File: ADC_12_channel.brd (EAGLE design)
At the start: 160 x 127 mm, 165 parts, among them K1 691131710003, K2 691101710002, K3 691101710002, K4 691101710002, K5 691101710002, K6 691101710002, K7 691101710002, K8 691101710002, K9 691101710002, U1 AD7864ASZ-1, U10 TL082D, U11 +12v, U12 V_REG_317SMD, U2 AD7864ASZ-1, U3 TL082D, U4 TL082D, U5 TL082D, U6 TL082D, U7 TL082D, U8 TL082D, U9 TL082D, X1 QTE-040

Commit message: Supply sorting commit
Sorted I/p +- 12V supply, 5V pending
changed Resistor package from 0805 to 1206 because its cheap, easy to handle, and easyly available

Update of R package done for 1st two input channels
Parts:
- removed U$1: LM3480IM4, SparkFun-PowerIC:SOT23-3
- removed U11: +12v, rathin_lib:TO-252
- added IC1: LM317BD2T, rathin_Vreg_D2pack:D2PACK
- added IC2: LM317BD2T, v-reg:D2PACK
- R11, R12, R13, R14, R15, R16, R24, R25, R26, R31, R36, R37: device resistor:M0805 -> resistor:M1206
- moved R57 10.6 mm to (76.7, -12.8), turned to 0 degrees
- moved C51 6.33 mm to (66.7, -15.7), turned to 0 degrees
- moved R56 5.28 mm to (72.1, -18.5), turned to 0 degrees
- moved C49 4.22 mm to (72.0, -15.8), turned to 180 degrees
- moved R59 3.91 mm to (66.7, -18.6)
- moved C48 2.70 mm to (76.7, -9.55)
- moved C43 2.53 mm to (69.8, 14.7)
- moved R50 2.39 mm to (109.0, 7.87)
- moved C52 1.15 mm to (60.6, -13.5)
- moved R55 0.94 mm to (76.7, -16.8)
- moved U10 0.31 mm to (96.3, -12.2)
- moved R53 0.25 mm to (113.8, 6.10)
- moved R65 0.24 mm to (94.5, -23.9)
- moved R41 0.18 mm to (66.1, 37.4)
- moved C45 0.17 mm to (95.2, 9.91)
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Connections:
- net GND2: now also IC1.1, IC2.2; no longer U$1.3, U11.1
- net N$35: now also IC1.3; no longer U11.3
- net N$36: now also IC2.1; no longer U$1.2
- net VCC_12+: now also IC2.3; no longer U$1.1
- net VCC_12-: now also IC1.2; no longer U11.2
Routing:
- net N$82: track 0.00 -> 22.6 mm
- net AGND: track 120.4 -> 131.8 mm
- net N$61: track 19.8 -> 11.6 mm
- net VDD: track 24.3 -> 16.3 mm
- net ADC8: track 0.00 -> 6.39 mm
- net VCC_12-: track 0.00 -> 4.94 mm
- net N$63: track 4.85 -> 0.00 mm
- net N$68: track 15.6 -> 14.3 mm
- net N$29: track 19.7 -> 18.9 mm

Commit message: R & C package update
Updated all R to 1206
Updated all input stage C of 0.1u to 0603 package
All 47uF to 1206 package
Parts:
- removed JP2, JP3, JP5: (no value), SparkFun-Retired:1X02
- added R74: 0, resistor:M1206
- C1, C10, C11, C12, C13, C14, C15, C16, C17, C18, C19, C2, C22, C30, C31, C32, C33, C34, C35, C36, C37, C38, C39, C40, C41, C42, C43, C44, C45, C46, C47, C48, C49, C5, C50, C51, C52, C53, C54, C55, C56, C57, C58, C59, C6, C9: device rcl:C0805 -> rcl:C0603K
- C4, C8: device rcl:C0603K -> rcl:C1206K
- R10, R27, R28, R29, R30, R32, R33, R34, R35, R38, R39, R40, R41, R42, R43, R44, R45, R47, R48, R49, R50, R51, R53, R54, R55, R56, R57, R59, R60, R61, R62, R63, R64, R65: device resistor:M0805 -> resistor:M1206
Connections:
- removed net N$18: JP2.2, JP3.1, U1.11
- removed net N$25: JP5.1, R72.1, U2.11
- net DGND: now also R74.2; no longer JP2.1
- net N$19: now also R74.1, U1.11; no longer JP3.2
- net N$26: now also R72.1, U2.11; no longer JP5.2
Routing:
- net N$61: track 11.6 -> 12.4 mm
- net N$68: track 14.3 -> 15.0 mm
- net N$60: track 20.4 -> 21.0 mm

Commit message: Supply Finally sorted out!
arranging supply components
Working on realigning resistors of input stage
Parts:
- added R75: 100k, rcl:R1206
- moved C22 442.6 mm to (228.9, 64.0)
- moved C59 442.6 mm to (228.9, 70.4)
- moved CONVST 442.6 mm to (221.2, 48.6)
- moved IC1 442.6 mm to (213.4, 39.8)
- moved IC2 442.6 mm to (201.4, 39.8)
- moved R20 442.6 mm to (221.7, 43.9)
- moved R71 442.6 mm to (221.7, 37.9)
- moved R73 442.6 mm to (221.7, 31.9)
- moved R74 442.6 mm to (197.9, 25.9)
- moved U12 442.6 mm to (222.6, 56.6)
- moved D1 378.0 mm to (140.2, 90.0)
- moved D2 374.9 mm to (140.6, 79.9)
- moved C21 330.3 mm to (176.6, 160.4)
- moved C26 330.3 mm to (150.0, 115.9)
- moved C28 330.3 mm to (174.1, 146.4)
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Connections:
- removed net 0.8V: R21.2, R22.1, R23.1
- new net 3V: R21.2, R22.1, R23.1, R75.2
- net VCC_5+: now also R75.1

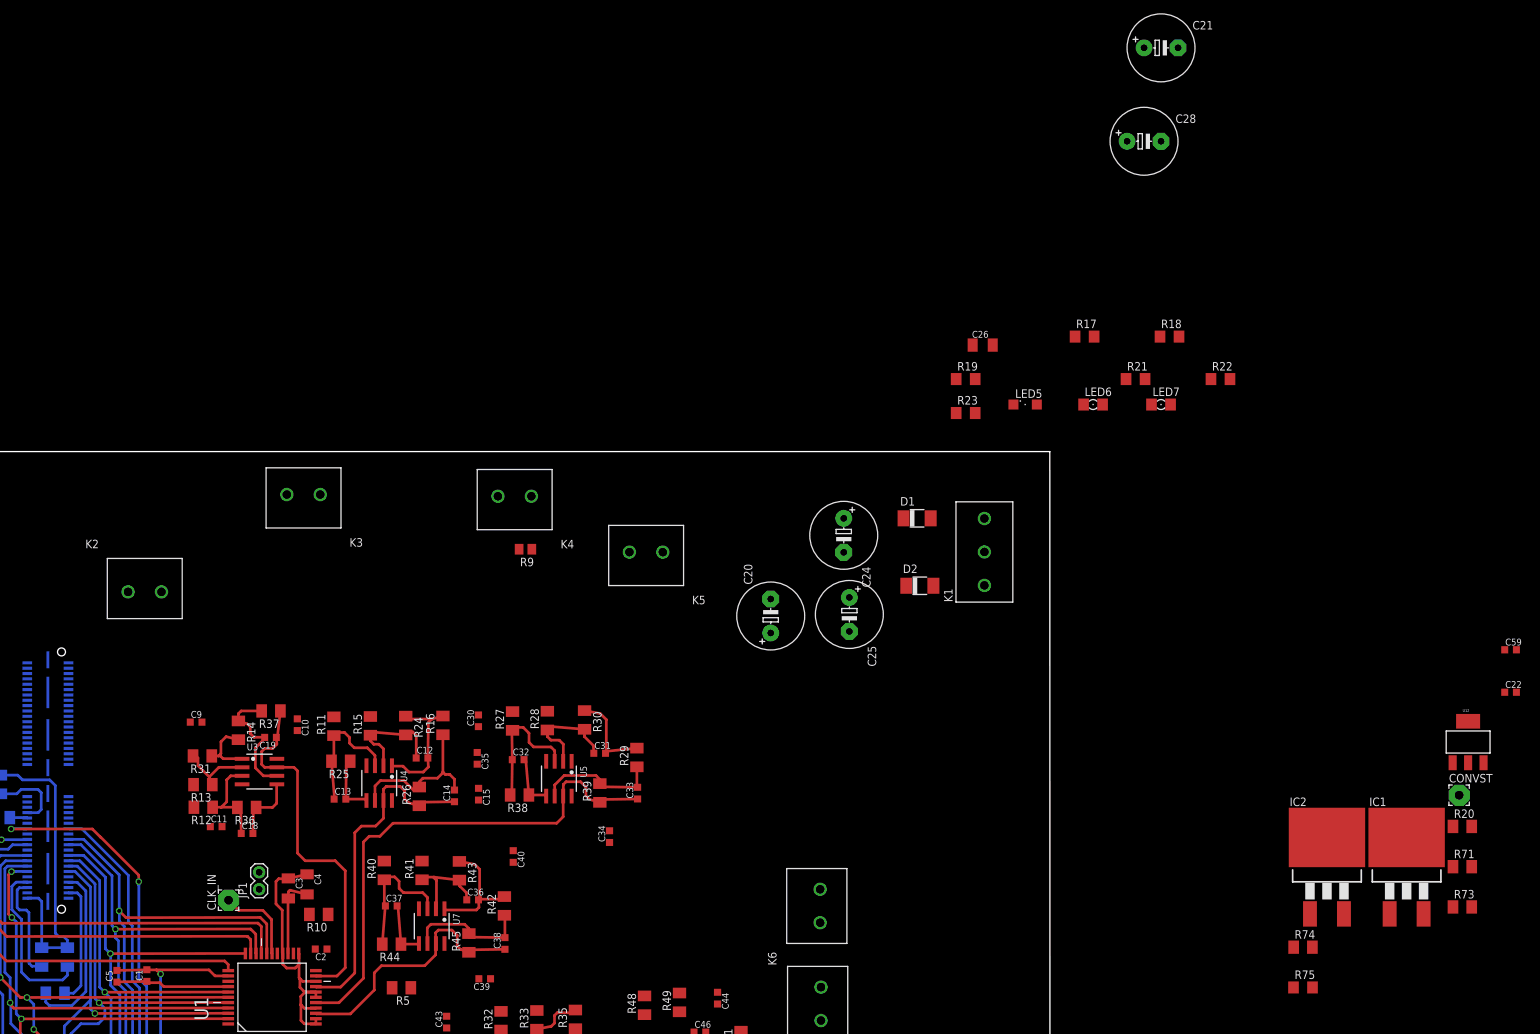
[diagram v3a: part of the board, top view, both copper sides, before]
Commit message: Layout of Supply DONE!
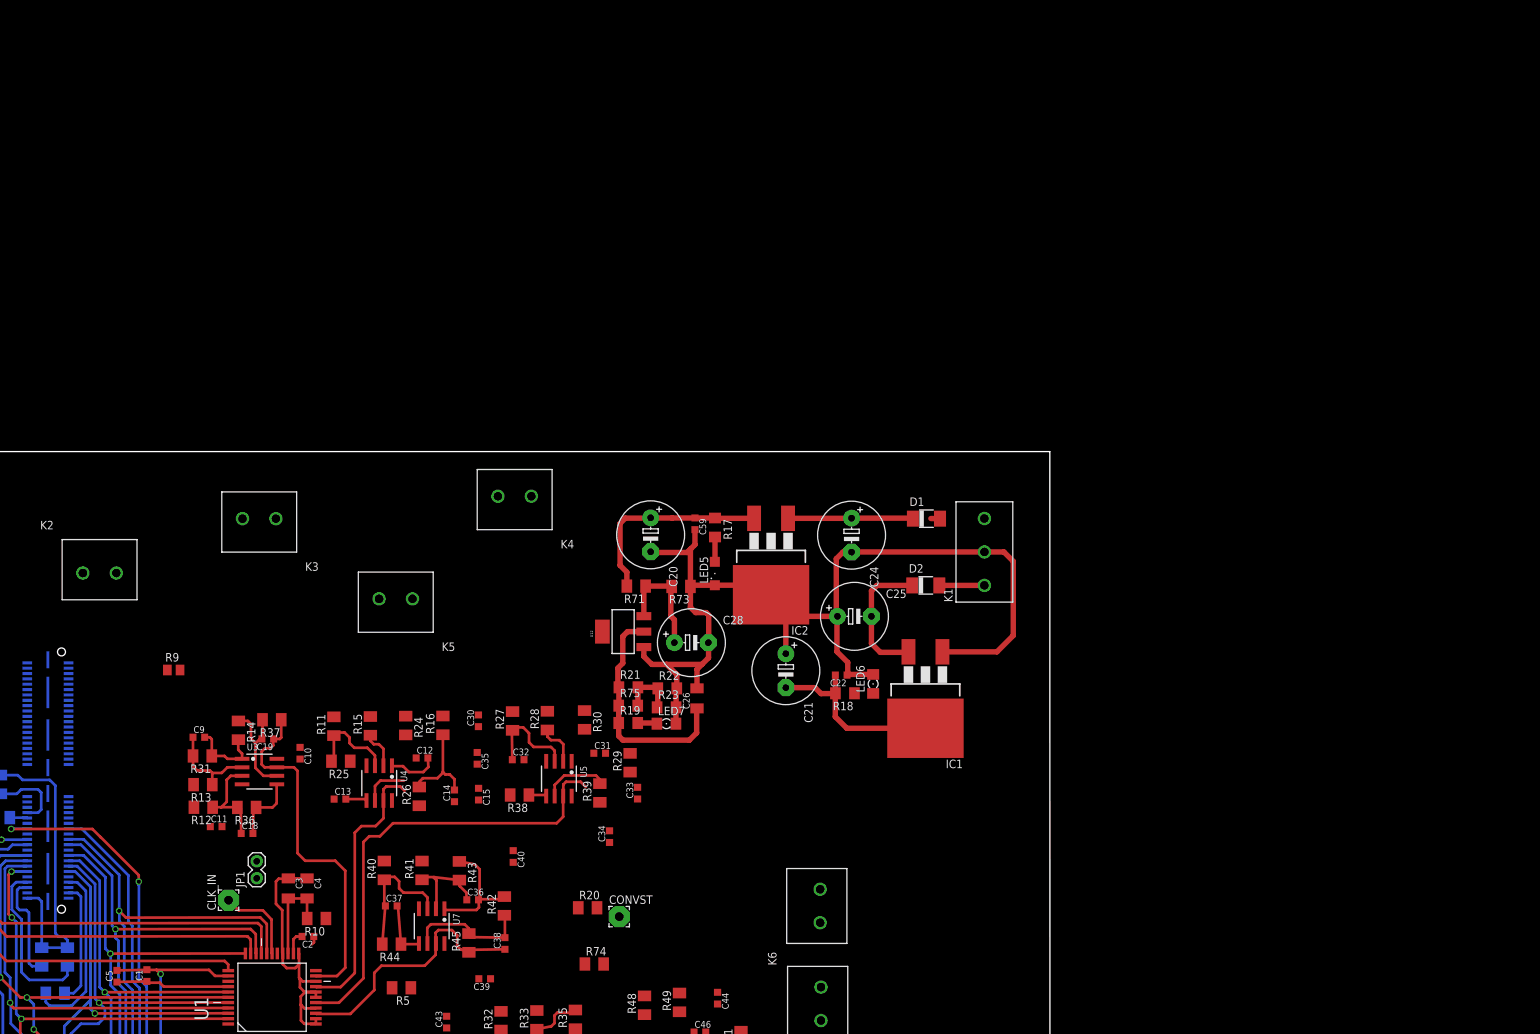
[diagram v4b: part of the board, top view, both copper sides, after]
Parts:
- moved R20 131.4 mm to (90.9, 31.8)
- moved R71 130.5 mm to (98.1, 79.9), turned to 180 degrees
- moved U12 127.4 mm to (96.2, 73.1), turned to 90 degrees
- moved CONVST 126.9 mm to (95.6, 30.5)
- moved R73 126.3 mm to (104.9, 79.8), turned to 180 degrees
- moved C59 123.4 mm to (106.9, 89.2), turned to 270 degrees
- moved R75 109.4 mm to (97.0, 62.0)
- moved C21 108.7 mm to (120.5, 67.2), turned to 270 degrees
- moved R74 106.0 mm to (91.9, 23.4)
- moved C28 101.0 mm to (106.4, 71.4)
- moved C22 100.1 mm to (128.8, 66.6), turned to 180 degrees
- moved R22 94.8 mm to (102.8, 64.6)
- moved IC2 92.9 mm to (118.3, 81.1), turned to 180 degrees
- moved R21 88.8 mm to (97.0, 64.7)
- moved LED7 88.0 mm to (102.7, 59.3)
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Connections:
- removed net GND2: C20.-, C21.+, C22.1, C24.-, C25.+, C26.2, C28.-, C59.2, IC1.1, IC2.2, K1.2, LED5.C, LED6.C, LED7.C, R22.2, R23.2, R73.1, U12.1
- net DGND: now also C20.-, C21.+, C22.1, C24.-, C25.+, C26.2, C28.-, C59.2, IC1.1, IC2.2, K1.2, LED5.C, LED6.C, LED7.C, R22.2, R23.2, R73.1, U12.1
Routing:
- net DGND: track 17.0 -> 172.8 mm
- net VCC_5+: track 0.00 -> 34.7 mm
- net VCC_12+: track 0.00 -> 30.2 mm
- net VCC_12-: track 5.01 -> 33.3 mm
- net N$35: track 0.00 -> 20.4 mm
- net N$36: track 0.00 -> 18.7 mm
- net 5V: track 0.00 -> 17.2 mm
- net N$59: track 13.6 -> 0.00 mm
- net N$34: track 19.6 -> 7.92 mm
- net N$58: track 17.4 -> 6.42 mm
- net N$33: track 16.8 -> 6.41 mm
- net AGND: track 131.8 -> 121.4 mm
- net ADC3: track 78.9 -> 69.6 mm
- net N$65: track 19.1 -> 9.88 mm
- net ADC2: track 50.2 -> 41.3 mm
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
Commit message: Conversion ST signal, supply & area
-Added isolating resistor in CONVST signal coming from header/processor
-Defined boundry of the baord
- Relocated and reorianted the supply
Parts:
- removed CONV_ST1: (no value), wirepad:3,17/1,3
- added CONV_ST2: (no value), wirepad:3,17/1,3
- added R76: 0, resistor:M1206
- moved C20 54.0 mm to (105.9, 33.8), turned to 0 degrees
- moved R71 50.6 mm to (113.6, 31.6), turned to 270 degrees
- moved U12 49.7 mm to (120.4, 29.7), turned to 180 degrees
- moved C59 48.8 mm to (104.2, 40.4), turned to 0 degrees
- moved R19 47.0 mm to (134.0, 30.5), turned to 90 degrees
- moved R75 46.7 mm to (131.4, 30.5), turned to 90 degrees
- moved R21 46.7 mm to (128.7, 30.5), turned to 90 degrees
- moved R17 45.5 mm to (104.8, 43.4), turned to 0 degrees
- moved R73 42.4 mm to (113.6, 38.4), turned to 270 degrees
- moved K1 41.8 mm to (108.5, 83.7), turned to 180 degrees
- moved D1 40.9 mm to (103.5, 75.1), turned to 90 degrees
- moved LED7 39.1 mm to (134.1, 36.2), turned to 90 degrees
- moved R23 38.7 mm to (131.7, 36.2), turned to 90 degrees
- moved R22 38.5 mm to (128.9, 36.3), turned to 90 degrees
- moved LED5 38.4 mm to (111.7, 43.4), turned to 180 degrees
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- renumbered CONVST to CONVST1
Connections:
- removed net N$42: CONVST1.1, R20.2
- new net N$18: CONVST1.1, R20.1, U1.3
- new net N$25: CONV_ST2.1, R76.1, U2.3
- net CONVST: now also R20.2, R76.2; no longer CONV_ST1.1, R20.1, U1.3, U2.3
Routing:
- net CONVST: track 0.00 -> 92.4 mm, vias 0 -> 3
- net VCC_3+: track 0.00 -> 43.8 mm, vias 0 -> 2
- net AGND: track 121.4 -> 111.1 mm
- net N$55: track 15.9 -> 8.27 mm
- net DVDD: track 53.5 -> 54.3 mm
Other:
- board size 160 x 127 mm -> 148.1 x 127 mm

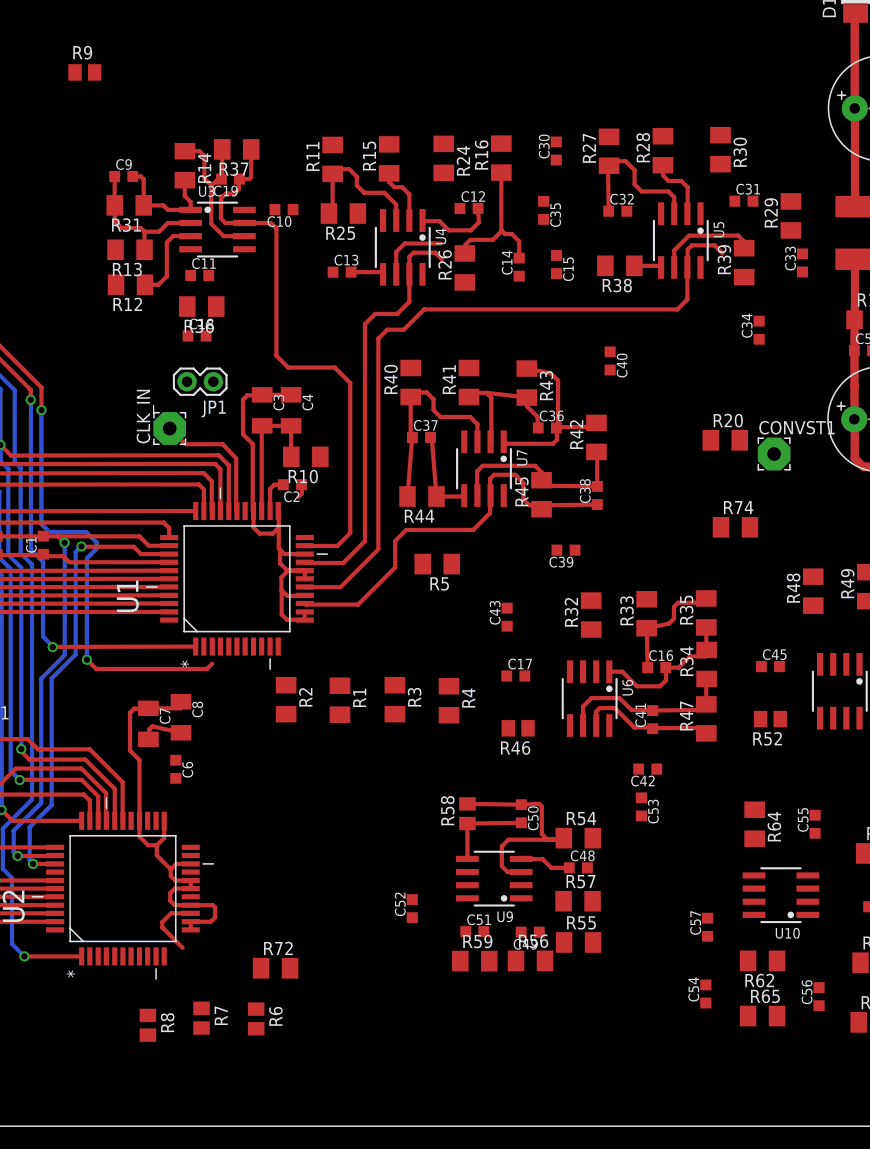
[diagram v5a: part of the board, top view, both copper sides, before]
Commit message: ADC-1 Opamp component arrangement FINALIZED!
Uniformly arranged all component of Opamps 1-4
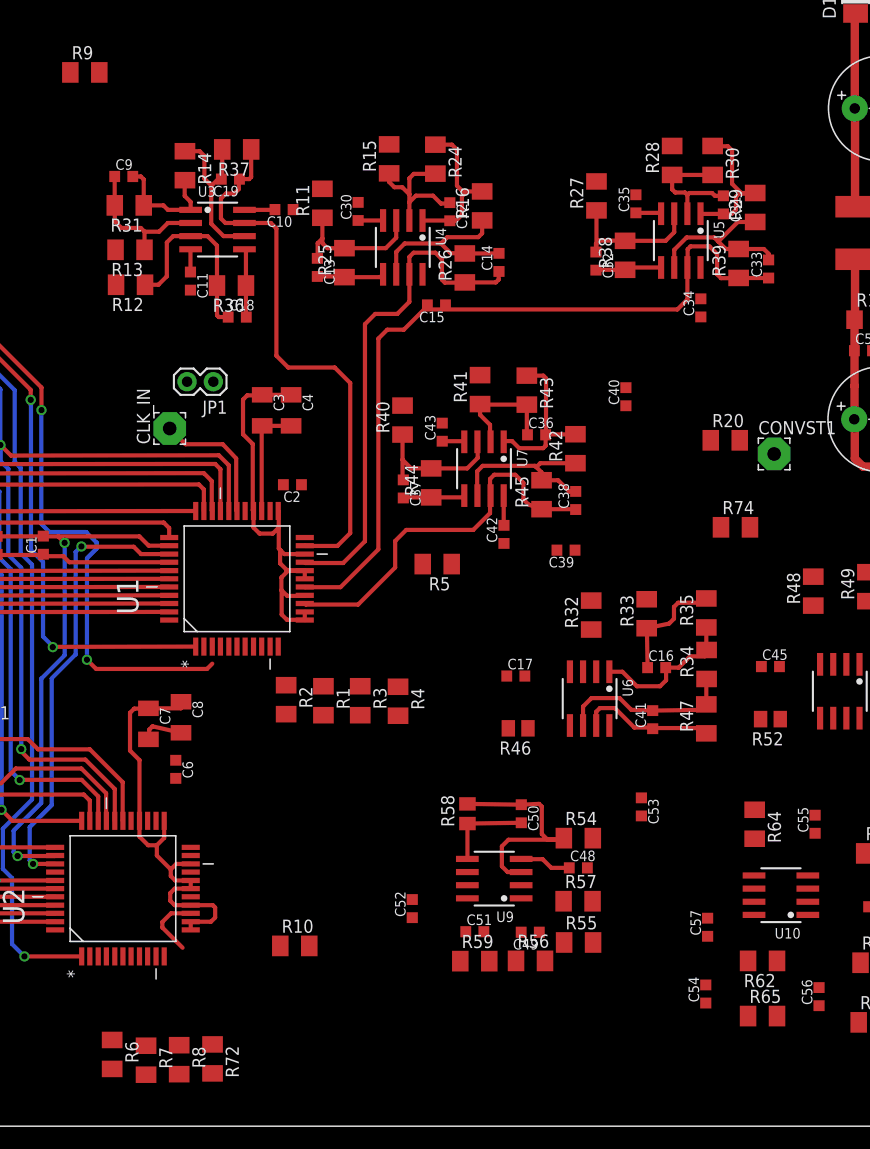
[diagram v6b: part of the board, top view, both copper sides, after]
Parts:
- R6, R7, R8, R9: device resistor:M0805 -> resistor:M1206
- moved R10 47.3 mm to (49.3, -17.1), turned to 0 degrees
- moved C42 26.6 mm to (69.5, 22.7), turned to 90 degrees
- moved C30 20.0 mm to (55.4, 53.9)
- moved C43 19.0 mm to (63.5, 32.6)
- moved R6 14.3 mm to (31.6, -27.6)
- moved C15 12.2 mm to (63.0, 44.9), turned to 180 degrees
- moved R72 10.7 mm to (41.3, -28.0), turned to 270 degrees
- moved C35 8.94 mm to (82.2, 54.6), turned to 90 degrees
- moved R7 6.73 mm to (34.9, -28.1)
- moved C34 6.04 mm to (88.5, 44.6)
- moved C37 5.28 mm to (59.8, 27.1), turned to 270 degrees
- moved C32 5.27 mm to (78.4, 49.1), turned to 270 degrees
- moved R16 4.98 mm to (67.4, 54.4)
- moved R4 4.93 mm to (59.3, 6.55)
- moved R25 4.75 mm to (54.1, 48.9), turned to 90 degrees
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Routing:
- net N$59: track 0.00 -> 14.7 mm
- net N$55: track 8.27 -> 19.1 mm
- net AGND: track 111.1 -> 121.0 mm
- net VCC_12-: track 33.3 -> 42.5 mm
- net N$33: track 6.41 -> 15.1 mm
- net ADC2: track 41.3 -> 49.3 mm
- net N$65: track 9.88 -> 16.9 mm
- net N$34: track 7.92 -> 14.9 mm
- net N$70: track 20.2 -> 14.0 mm
- net ADC3: track 69.6 -> 75.7 mm
- net N$58: track 6.42 -> 12.5 mm
- net VCC_12+: track 30.2 -> 36.1 mm
- net N$16: track 3.59 -> 0.00 mm
- net N$68: track 15.0 -> 11.6 mm
- net N$46: track 21.9 -> 18.5 mm
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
